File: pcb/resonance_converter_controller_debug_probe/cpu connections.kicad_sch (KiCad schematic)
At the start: 1 part, among them U30 OSD32MP157C-512M-BAA

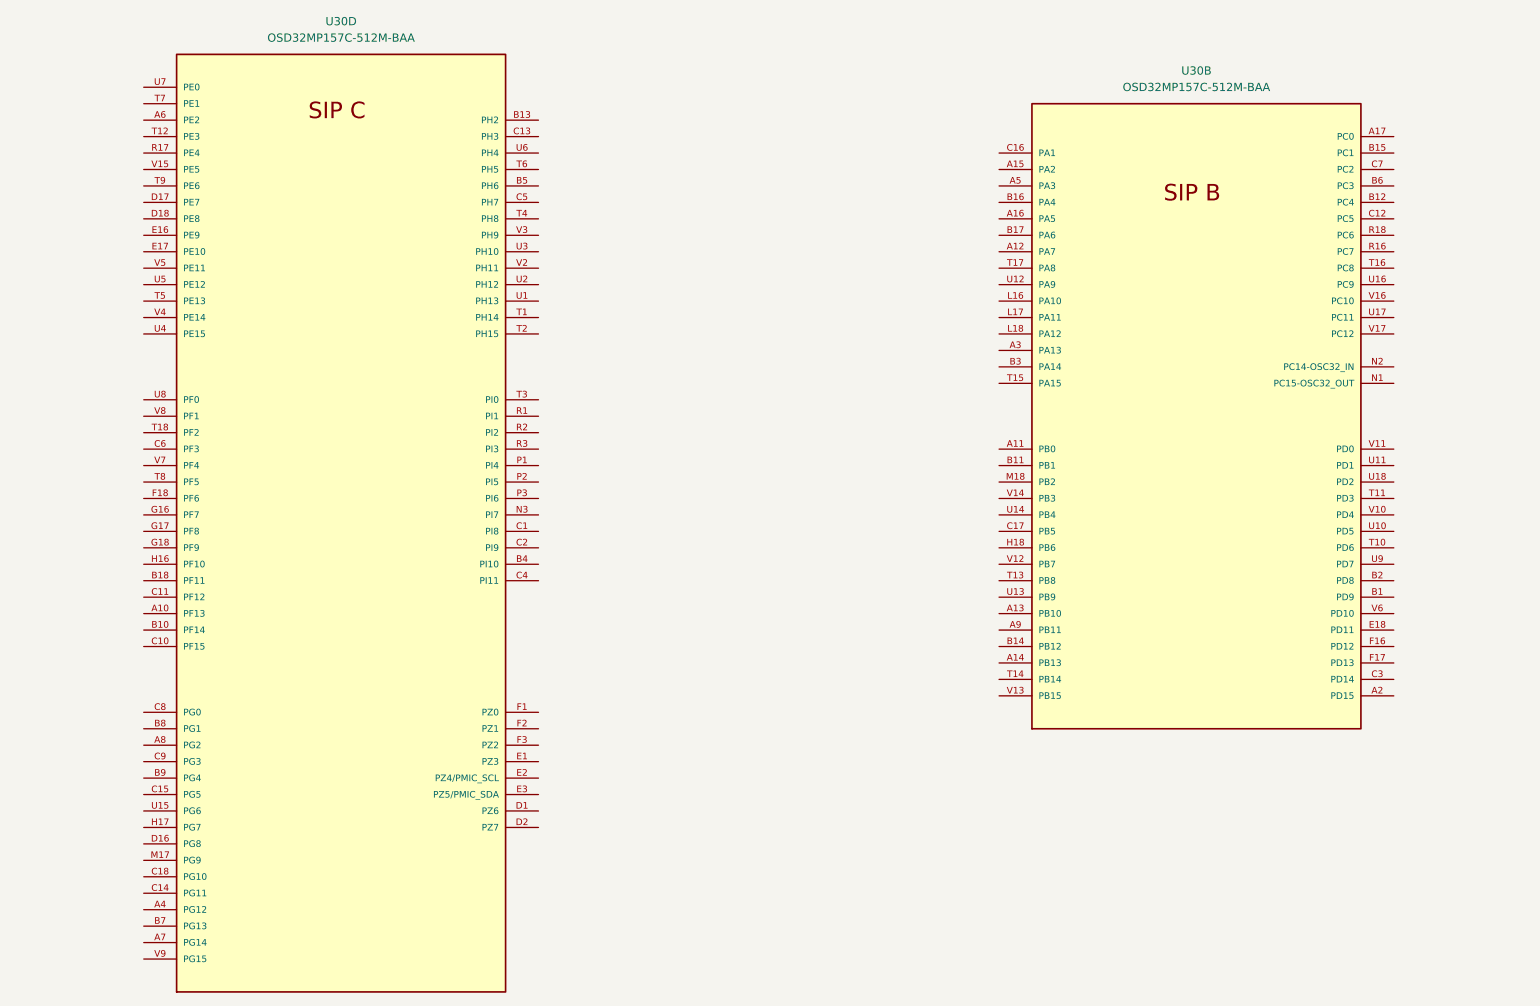
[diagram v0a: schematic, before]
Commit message: Add schematic for debug probe
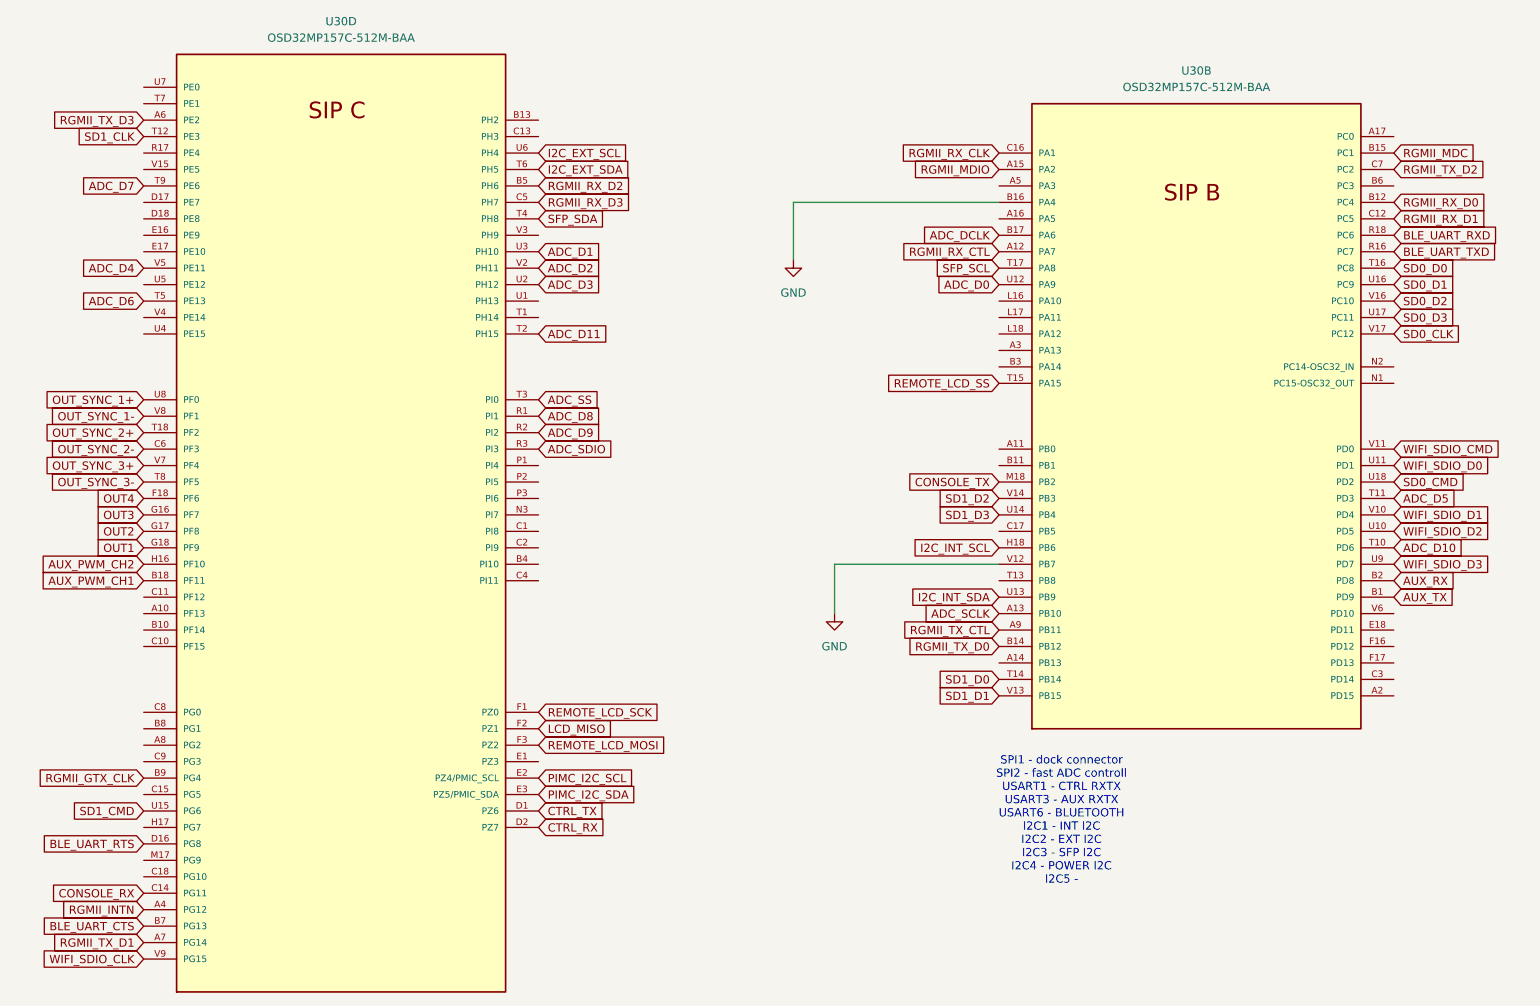
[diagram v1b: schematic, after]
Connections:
- net RGMII_RX_CTL: now reaches U30.A12 (PA7)
- net ADC_SCLK: now reaches U30.A13 (PB10)
- net RGMII_MDIO: now reaches U30.A15 (PA2)
- net RGMII_TX_CTL: now reaches U30.A9 (PB11)
- net AUX_TX: now reaches U30.B1 (PD9)
- net RGMII_RX_D0: now reaches U30.B12 (PC4)
- net RGMII_TX_D0: now reaches U30.B14 (PB12)
- net RGMII_MDC: now reaches U30.B15 (PC1)
- net GND: now reaches U30.B16 (PA4)
- net GND: now also U30.V12 (PB7)
- net ADC_DCLK: now reaches U30.B17 (PA6)
- net AUX_RX: now reaches U30.B2 (PD8)
- net RGMII_RX_D1: now reaches U30.C12 (PC5)
- net RGMII_RX_CLK: now reaches U30.C16 (PA1)
- net RGMII_TX_D2: now reaches U30.C7 (PC2)
- net I2C_INT_SCL: now reaches U30.H18 (PB6)
- net CONSOLE_TX: now reaches U30.M18 (PB2)
- net BLE_UART_TXD: now reaches U30.R16 (PC7)
- net BLE_UART_RXD: now reaches U30.R18 (PC6)
- net ADC_D10: now reaches U30.T10 (PD6)
- net ADC_D5: now reaches U30.T11 (PD3)
- net SD1_D0: now reaches U30.T14 (PB14)
- net REMOTE_LCD_SS: now reaches U30.T15 (PA15)
- net SD0_D0: now reaches U30.T16 (PC8)
- net SFP_SCL: now reaches U30.T17 (PA8)
- net WIFI_SDIO_D2: now reaches U30.U10 (PD5)
- net WIFI_SDIO_D0: now reaches U30.U11 (PD1)
- net ADC_D0: now reaches U30.U12 (PA9)
- net I2C_INT_SDA: now reaches U30.U13 (PB9)
- net SD1_D3: now reaches U30.U14 (PB4)
- net SD0_D1: now reaches U30.U16 (PC9)
- net SD0_D3: now reaches U30.U17 (PC11)
- net SD0_CMD: now reaches U30.U18 (PD2)
- net WIFI_SDIO_D3: now reaches U30.U9 (PD7)
- net WIFI_SDIO_D1: now reaches U30.V10 (PD4)
- net WIFI_SDIO_CMD: now reaches U30.V11 (PD0)
- net SD1_D1: now reaches U30.V13 (PB15)
- net SD1_D2: now reaches U30.V14 (PB3)
- net SD0_D2: now reaches U30.V16 (PC10)
- net SD0_CLK: now reaches U30.V17 (PC12)
- net RGMII_INTN: now reaches U30.A4 (PG12)
- net RGMII_TX_D3: now reaches U30.A6 (PE2)
- net RGMII_TX_D1: now reaches U30.A7 (PG14)
- net AUX_PWM_CH1: now reaches U30.B18 (PF11)
- net RGMII_RX_D2: now reaches U30.B5 (PH6)
- net BLE_UART_CTS: now reaches U30.B7 (PG13)
- net RGMII_GTX_CLK: now reaches U30.B9 (PG4)
- net CONSOLE_RX: now reaches U30.C14 (PG11)
- net RGMII_RX_D3: now reaches U30.C5 (PH7)
- net OUT_SYNC_2-: now reaches U30.C6 (PF3)
- net CTRL_TX: now reaches U30.D1 (PZ6)
- net BLE_UART_RTS: now reaches U30.D16 (PG8)
- net CTRL_RX: now reaches U30.D2 (PZ7)
- net PIMC_I2C_SCL: now reaches U30.E2 (PZ4/PMIC_SCL)
- net PIMC_I2C_SDA: now reaches U30.E3 (PZ5/PMIC_SDA)
- net REMOTE_LCD_SCK: now reaches U30.F1 (PZ0)
- net OUT4: now reaches U30.F18 (PF6)
- net LCD_MISO: now reaches U30.F2 (PZ1)
- net REMOTE_LCD_MOSI: now reaches U30.F3 (PZ2)
- net OUT3: now reaches U30.G16 (PF7)
- net OUT2: now reaches U30.G17 (PF8)
- net OUT1: now reaches U30.G18 (PF9)
- net AUX_PWM_CH2: now reaches U30.H16 (PF10)
- net ADC_D8: now reaches U30.R1 (PI1)
- net ADC_D9: now reaches U30.R2 (PI2)
- net ADC_SDIO: now reaches U30.R3 (PI3)
- net SD1_CLK: now reaches U30.T12 (PE3)
- net OUT_SYNC_2+: now reaches U30.T18 (PF2)
- net ADC_D11: now reaches U30.T2 (PH15)
- net ADC_SS: now reaches U30.T3 (PI0)
- net SFP_SDA: now reaches U30.T4 (PH8)
- net ADC_D6: now reaches U30.T5 (PE13)
- net I2C_EXT_SDA: now reaches U30.T6 (PH5)
- net OUT_SYNC_3-: now reaches U30.T8 (PF5)
- net ADC_D7: now reaches U30.T9 (PE6)
- net SD1_CMD: now reaches U30.U15 (PG6)
- net ADC_D3: now reaches U30.U2 (PH12)
- net ADC_D1: now reaches U30.U3 (PH10)
- net I2C_EXT_SCL: now reaches U30.U6 (PH4)
- net OUT_SYNC_1+: now reaches U30.U8 (PF0)
- net ADC_D2: now reaches U30.V2 (PH11)
- net ADC_D4: now reaches U30.V5 (PE11)
- net OUT_SYNC_3+: now reaches U30.V7 (PF4)
- net OUT_SYNC_1-: now reaches U30.V8 (PF1)
- net WIFI_SDIO_CLK: now reaches U30.V9 (PG15)
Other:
- note added: "SPI1 - dock connector SPI2 - fast ADC controll USART1 - CTRL RXTX USART3 - AUX RXTX USART6 - BLUETOOTH I2C1 - INT I2C I2C2 - EXT I2C I2C3 - SFP I2C I2C4 - POWER I2C I2C5 -"
